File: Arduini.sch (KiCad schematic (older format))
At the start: 0 parts

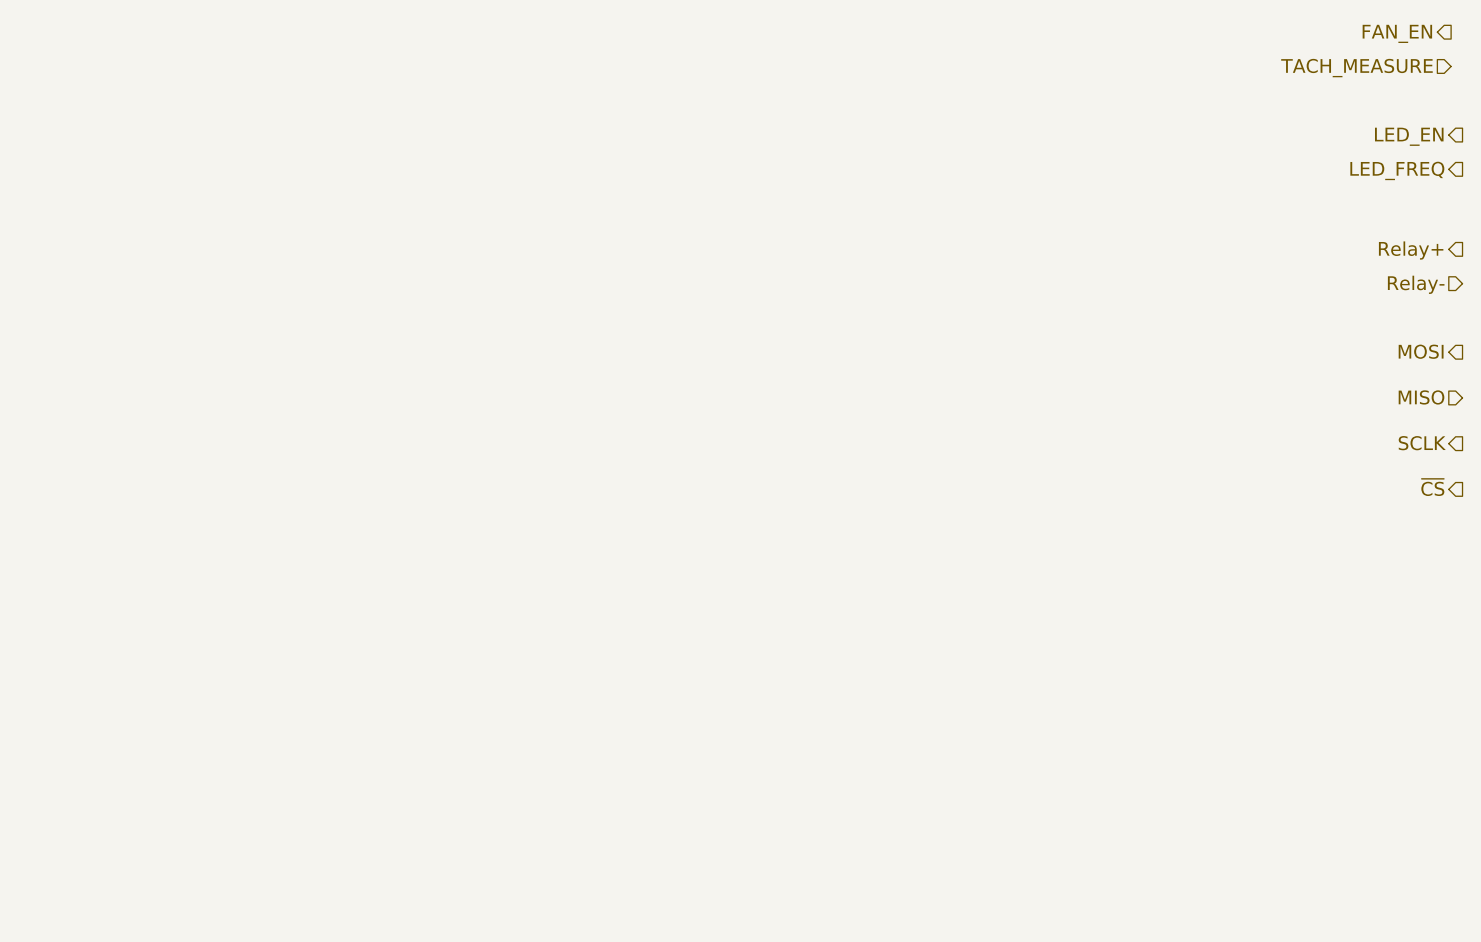
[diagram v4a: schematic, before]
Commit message: Arduino Module Connection
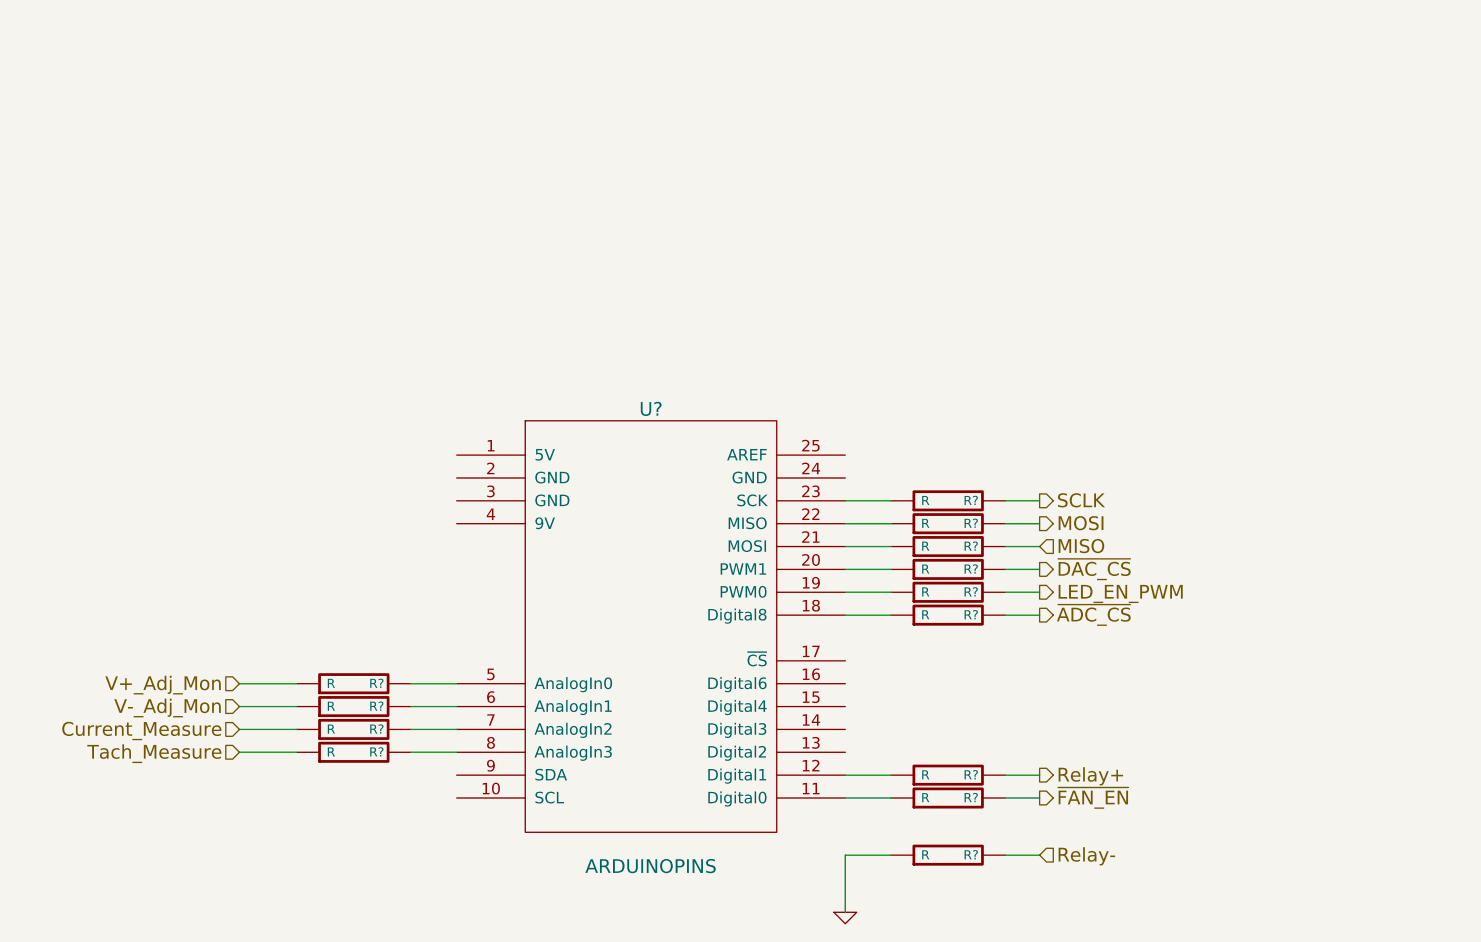
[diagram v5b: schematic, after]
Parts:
- added R? (x13): R, ~, symbol R
- added U?: ARDUINOPINS, symbol ARDUINOPINS
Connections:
- net MISO: now also R?.2
- net MOSI: now also R?.2
- net Relay+: now also R?.2
- net Relay-: now also R?.2
- net SCLK: now also R?.2
- new net: R?.1, U?.11 (Digital0)
- new net: R?.1, U?.12 (Digital1)
- new net: R?.1, U?.18 (Digital8)
- new net: R?.1, U?.19 (PWM0)
- new net: R?.1, U?.20 (PWM1)
- new net: R?.1, U?.21 (MOSI)
- new net: R?.1, U?.22 (MISO)
- new net: R?.1, U?.23 (SCK)
- new net: R?.2, U?.5 (AnalogIn0)
- new net: R?.2, U?.6 (AnalogIn1)
- new net: R?.2, U?.7 (AnalogIn2)
- new net: R?.2, U?.8 (AnalogIn3)
- new net Current_Measure: R?.1
- new net GND: R?.1
- new net LED_EN_PWM: R?.2
- new net Tach_Measure: R?.1
- new net V+_Adj_Mon: R?.1
- new net V-_Adj_Mon: R?.1
- new net ~ADC_CS: R?.2
- new net ~DAC_CS: R?.2
- new net ~FAN_EN: R?.2

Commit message: Fan/Current Module Refactor
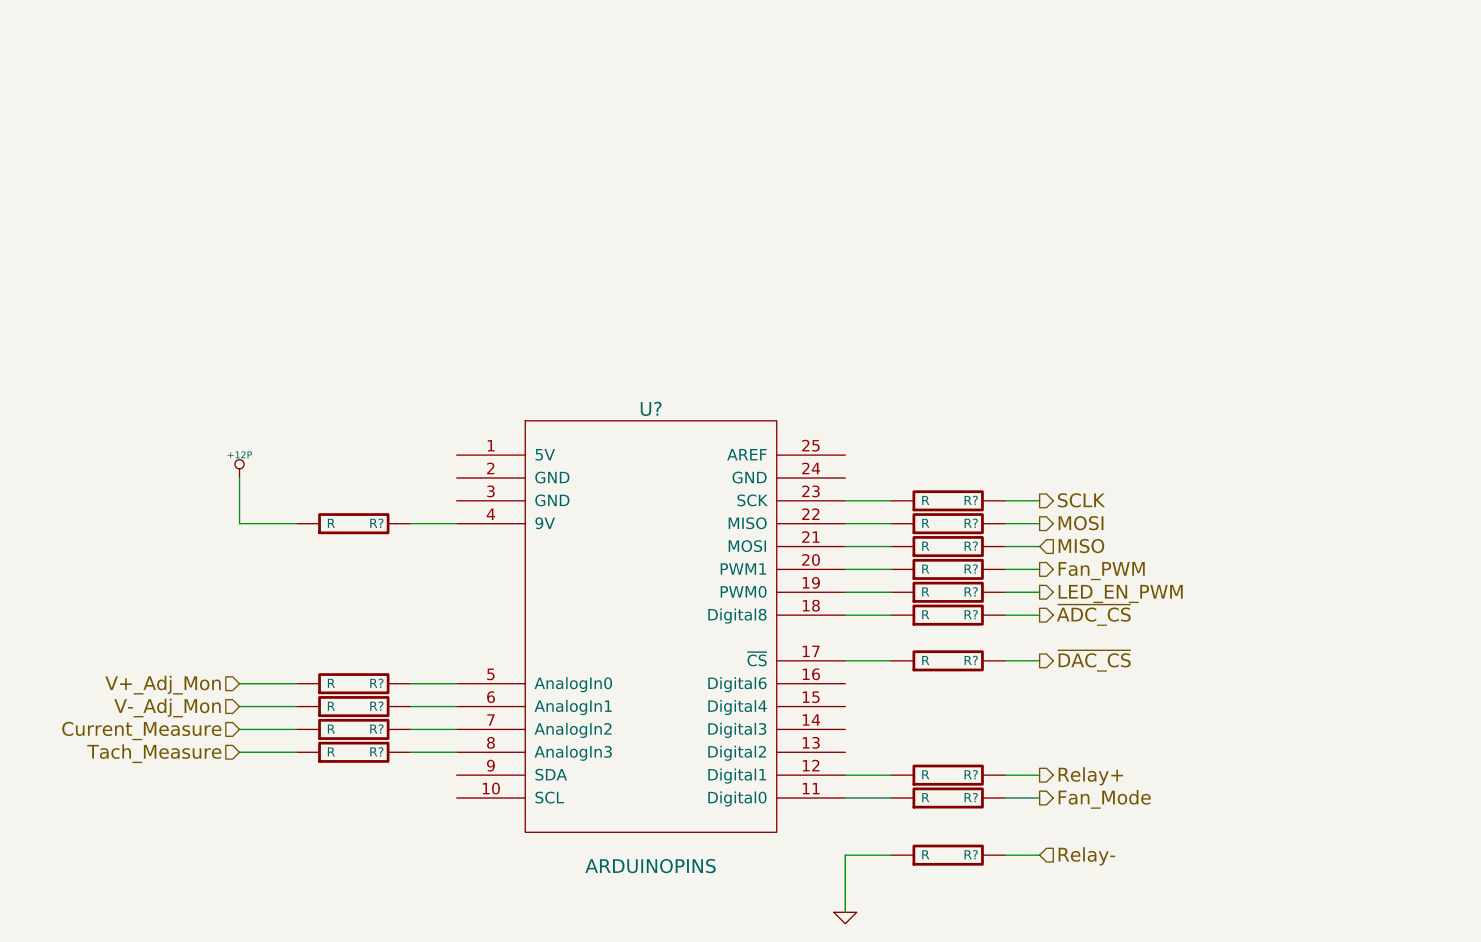
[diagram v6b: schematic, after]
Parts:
- added R? (x2): R, ~, symbol R
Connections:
- net at U?.17 (~CS): now also R?.1
- net at U?.20 (PWM1): now also R?.1; no longer R?.1
- net at U?.4 (9V): now also R?.2
- net ~FAN_EN renamed Fan_Mode
- new net +12P: R?.1
- new net Fan_PWM: R?.2
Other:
- moved on the sheet: R?
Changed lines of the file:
@@
 Sheet 8 9
 Title ""
-Date "22 oct 2013"
+Date "23 oct 2013"
 Rev ""
 Comp ""
@@
 Text HLabel 7650 2750 2    60   Output ~ 0
 SCLK
-Text HLabel 7650 3050 2    60   Output ~ 0
+Text HLabel 7650 3450 2    60   Output ~ 0
 ~DAC_CS
 Text HLabel 7650 3150 2    60   Output ~ 0
 LED_EN_PWM
 Text HLabel 7650 4050 2    60   Output ~ 0
-~FAN_EN
+Fan_Mode
 Text HLabel 4150 3850 0    60   Input ~ 0
 Tach_Measure
@@
 L R R?
 U 1 1 5267993F
-P 7250 3050
-F 0 "R?" V 7250 2950 40  0000 C CNN
-F 1 "R" V 7250 3150 40  0000 C CNN
-F 2 "~" V 7180 3050 30  0000 C CNN
-F 3 "~" H 7250 3050 30  0000 C CNN
-	1    7250 3050
+P 7250 3450
+F 0 "R?" V 7250 3350 40  0000 C CNN
+F 1 "R" V 7250 3550 40  0000 C CNN
+F 2 "~" V 7180 3450 30  0000 C CNN
+F 3 "~" H 7250 3450 30  0000 C CNN
+	1    7250 3450
 	0    -1   -1   0
 $EndComp
@@
 	6800 2950 7000 2950
 Wire Wire Line
-	7000 3050 6800 3050
-Wire Wire Line
 	7500 2750 7650 2750
 Wire Wire Line
@@
 Wire Wire Line
 	7500 2950 7650 2950
-Wire Wire Line
-	7650 3050 7500 3050
 $Comp
 L R R?
@@
 Wire Wire Line
 	7650 3250 7500 3250
+Wire Wire Line
+	7650 3450 7500 3450
+Text HLabel 7650 3050 2    60   Output ~ 0
+Fan_PWM
+Wire Wire Line
+	6800 3450 7000 3450
+$Comp
+L R R?
+U 1 1 526C9148
+P 7250 3050
+F 0 "R?" V 7250 2950 40  0000 C CNN
+F 1 "R" V 7250 3150 40  0000 C CNN
+F 2 "~" V 7180 3050 30  0000 C CNN
+F 3 "~" H 7250 3050 30  0000 C CNN
+	1    7250 3050
+	0    -1   -1   0
+$EndComp
+Wire Wire Line
+	6800 3050 7000 3050
+Wire Wire Line
+	7500 3050 7650 3050
+$Comp
+L R R?
+U 1 1 526C9681
+P 4650 2850
+F 0 "R?" V 4650 2750 40  0000 C CNN
+F 1 "R" V 4650 2950 40  0000 C CNN
+F 2 "~" V 4580 2850 30  0000 C CNN
+F 3 "~" H 4650 2850 30  0000 C CNN
+	1    4650 2850
+	0    -1   -1   0
+$EndComp
+Wire Wire Line
+	4900 2850 5100 2850
+$Comp
+L +12P #PWR?
+U 1 1 526C96A7
+P 4150 2650
+F 0 "#PWR?" H 4150 2620 30  0001 C CNN
+F 1 "+12P" H 4150 2750 30  0000 C CNN
+F 2 "~" H 4150 2650 60  0000 C CNN
+F 3 "~" H 4150 2650 60  0000 C CNN
+	1    4150 2650
+	1    0    0    -1
+$EndComp
+Wire Wire Line
+	4400 2850 4150 2850
+Wire Wire Line
+	4150 2850 4150 2650
 $EndSCHEMATC
